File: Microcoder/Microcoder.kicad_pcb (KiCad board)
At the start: 2 copper layers, 12 x 12 mm, 7 parts, among them IC101 AS5600-ASOT, J101 Conn_01x04

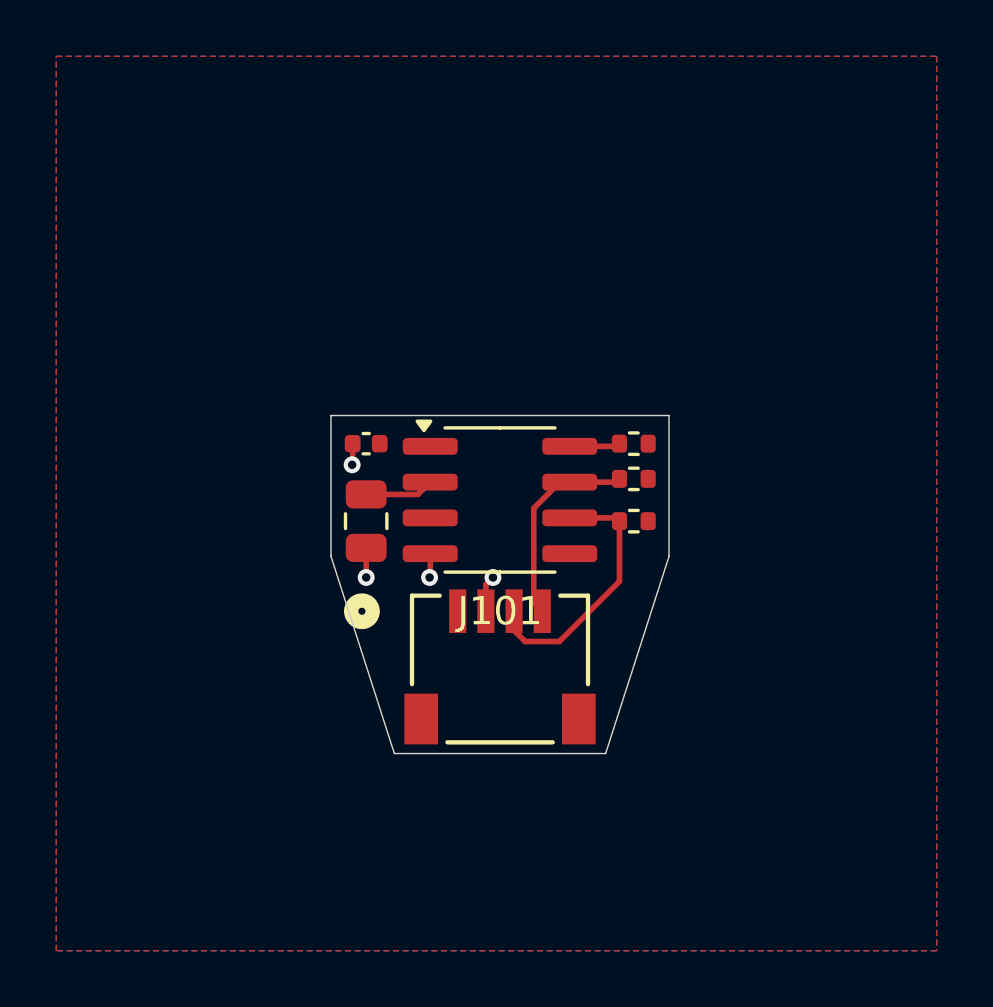
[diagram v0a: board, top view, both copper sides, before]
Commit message: Fixed issues preparing for build
Fixed XT30 connectors on Hydra_Driver reversed, fixed I2C connector pin order, refined silkscreens
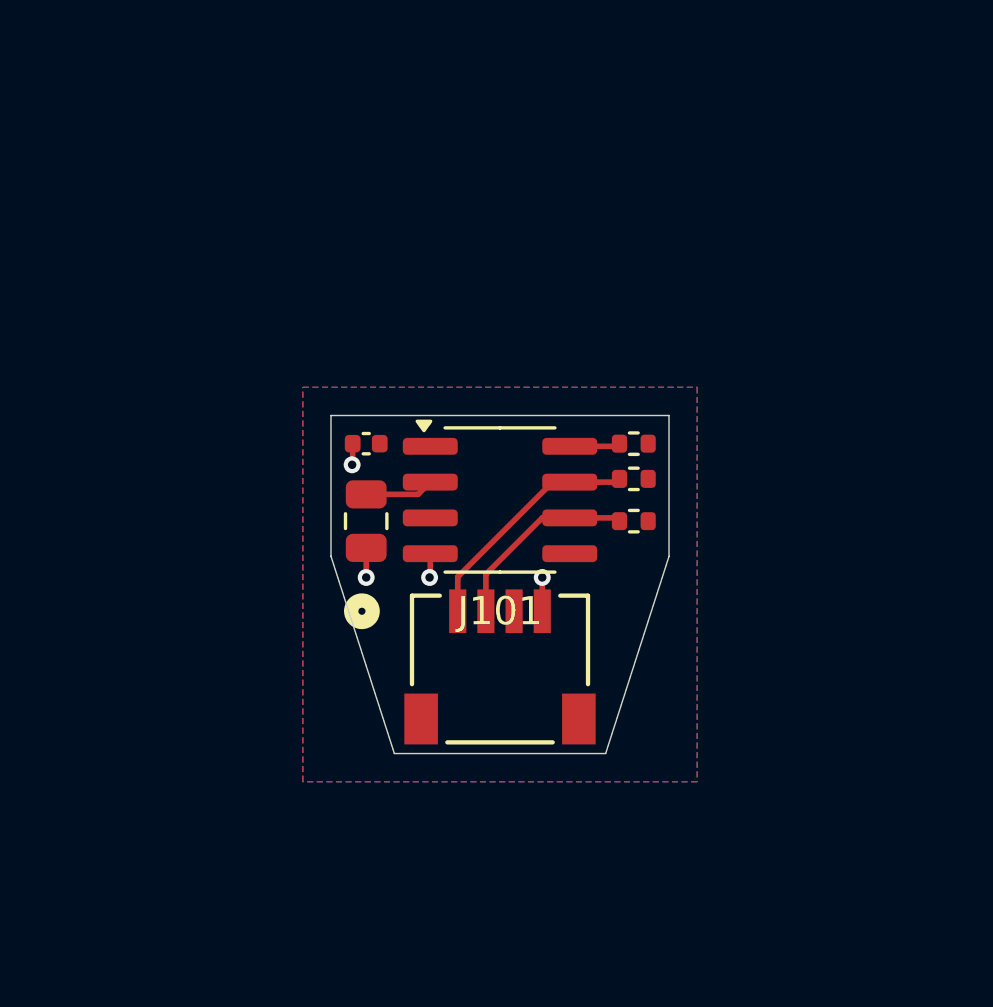
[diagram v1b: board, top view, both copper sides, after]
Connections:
- J101 pad 1: +3.3V -> /SCL
- J101 pad 2: GND -> /SDA
- J101 pad 3: /SDA -> +3.3V
- J101 pad 4: /SCL -> GND
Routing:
- net /SDA: track 9.42 -> 6.93 mm
- net /SCL: track 7.25 -> 8.40 mm
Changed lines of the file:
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@@
 			(size 0.6096 1.5494)
 			(layers "F.Cu" "F.Mask" "F.Paste")
-			(net 1 "+3.3V")
+			(net 3 "/SCL")
 			(pinfunction "Pin_1")
 			(pintype "passive")
@@
 			(size 0.6096 1.5494)
 			(layers "F.Cu" "F.Mask" "F.Paste")
-			(net 2 "GND")
+			(net 7 "/SDA")
 			(pinfunction "Pin_2")
 			(pintype "passive")
@@
 			(size 0.6096 1.5494)
 			(layers "F.Cu" "F.Mask" "F.Paste")
-			(net 7 "/SDA")
+			(net 1 "+3.3V")
 			(pinfunction "Pin_3")
 			(pintype "passive")
@@
 			(size 0.6096 1.5494)
 			(layers "F.Cu" "F.Mask" "F.Paste")
-			(net 3 "/SCL")
+			(net 2 "GND")
 			(pinfunction "Pin_4")
 			(pintype "passive")
@@
 	)
 	(segment
-		(start -0.499999 3.9485)
-		(end -0.499999 2.999999)
-		(width 0.2)
-		(layer "F.Cu")
-		(net 2)
-	)
-	(segment
 		(start -4.75 1.7)
 		(end -4.75 2.75)
@@
 	)
 	(segment
-		(start -0.499999 2.999999)
-		(end -0.25 2.75)
+		(start 1.5 3.9485)
+		(end 1.5 2.75)
 		(width 0.2)
 		(layer "F.Cu")
@@
 	)
 	(via
+		(at 1.5 2.75)
+		(size 0.6)
+		(drill 0.3)
+		(layers "F.Cu" "B.Cu")
+		(net 2)
+	)
+	(via
 		(at -4.75 2.75)
 		(size 0.6)
@@
 		(net 2)
 	)
-	(via
-		(at -0.25 2.75)
-		(size 0.6)
-		(drill 0.3)
-		(layers "F.Cu" "B.Cu")
-		(net 2)
-	)
 	(segment
 		(start 2.475 -0.635)
@@
 	)
 	(segment
-		(start 1.199 3.6475)
-		(end 1.199 0.294032)
+		(start 1.865 -0.635)
+		(end -1.5 2.73)
 		(width 0.2)
 		(layer "F.Cu")
@@
 	)
 	(segment
-		(start 1.5 3.9485)
-		(end 1.199 3.6475)
+		(start 2.475 -0.635)
+		(end 1.865 -0.635)
+		(width 0.2)
+		(layer "F.Cu")
+		(net 3)
+	)
+	(segment
+		(start -1.5 2.73)
+		(end -1.5 3.9485)
 		(width 0.2)
 		(layer "F.Cu")
@@
 	)
 	(segment
-		(start 2.128032 -0.635)
-		(end 2.475 -0.635)
-		(width 0.2)
-		(layer "F.Cu")
-		(net 3)
-	)
-	(segment
-		(start 1.199 0.294032)
-		(end 2.128032 -0.635)
-		(width 0.2)
-		(layer "F.Cu")
-		(net 3)
-	)
-	(segment
 		(start 2.475 -1.905)
 		(end 4.145 -1.905)
@@
 	)
 	(segment
-		(start 0.499999 4.629999)
-		(end 0.8942 5.0242)
-		(width 0.2)
-		(layer "F.Cu")
-		(net 7)
-	)
-	(segment
-		(start 4.24 2.89)
-		(end 4.24 0.75)
-		(width 0.2)
-		(layer "F.Cu")
-		(net 7)
-	)
-	(segment
 		(start 2.475 0.635)
 		(end 4.125 0.635)
@@
 	)
 	(segment
-		(start 0.8942 5.0242)
-		(end 2.1058 5.0242)
-		(width 0.2)
-		(layer "F.Cu")
-		(net 7)
-	)
-	(segment
-		(start 2.1058 5.0242)
-		(end 4.24 2.89)
-		(width 0.2)
-		(layer "F.Cu")
-		(net 7)
-	)
-	(segment
 		(start 4.125 0.635)
 		(end 4.24 0.75)
@@
 	)
 	(segment
-		(start 0.499999 3.9485)
-		(end 0.499999 4.629999)
+		(start -0.499999 2.635)
+		(end -0.499999 3.9485)
+		(width 0.2)
+		(layer "F.Cu")
+		(net 7)
+	)
+	(segment
+		(start 1.500001 0.635)
+		(end -0.499999 2.635)
+		(width 0.2)
+		(layer "F.Cu")
+		(net 7)
+	)
+	(segment
+		(start 2.475 0.635)
+		(end 1.500001 0.635)
 		(width 0.2)
 		(layer "F.Cu")
@@
 		(polygon
 			(pts
-				(xy -15.75 -15.75) (xy 15.5 -15.75) (xy 15.5 16) (xy -15.75 16)
+				(xy -7 -4) (xy 7 -4) (xy 7 10) (xy -7 10)
 			)
 		)
@@
 		(polygon
 			(pts
-				(xy -15.75 -15.75) (xy 15.5 -15.75) (xy 15.5 16) (xy -15.75 16)
-			)
-		)
+				(xy -7 -4) (xy 7 -4) (xy 7 10) (xy -7 10)
+			)
+		)

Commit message: More changes to start production
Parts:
- removed R103: 10k, Resistor_SMD:R_0402_1005Metric
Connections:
- IC101 pad 8: Net-(IC101-DIR) -> GND
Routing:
- net Net-(IC101-DIR): track 1.80 -> 0.00 mm
- net GND: track 3.86 -> 5.63 mm, vias 4 -> 5
